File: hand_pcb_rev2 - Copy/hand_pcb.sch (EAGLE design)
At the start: 70 parts

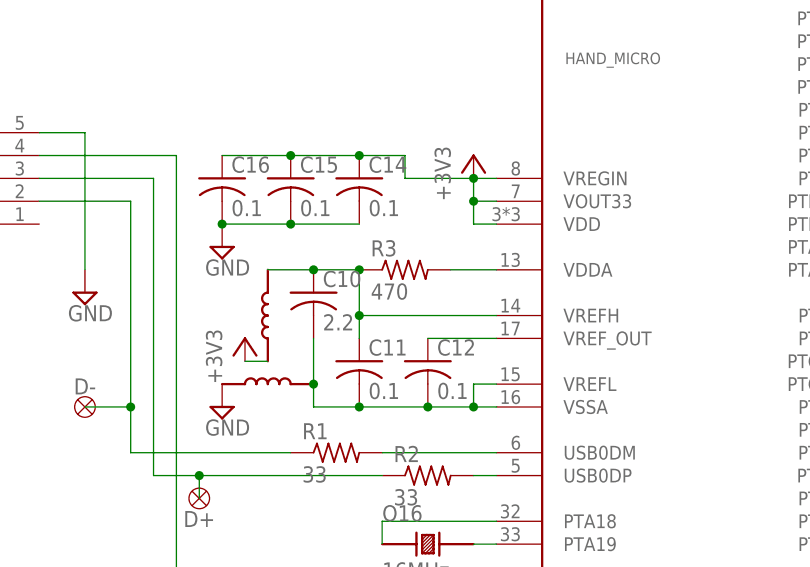
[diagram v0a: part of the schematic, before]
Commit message: corrected some resistors and caps for the M04
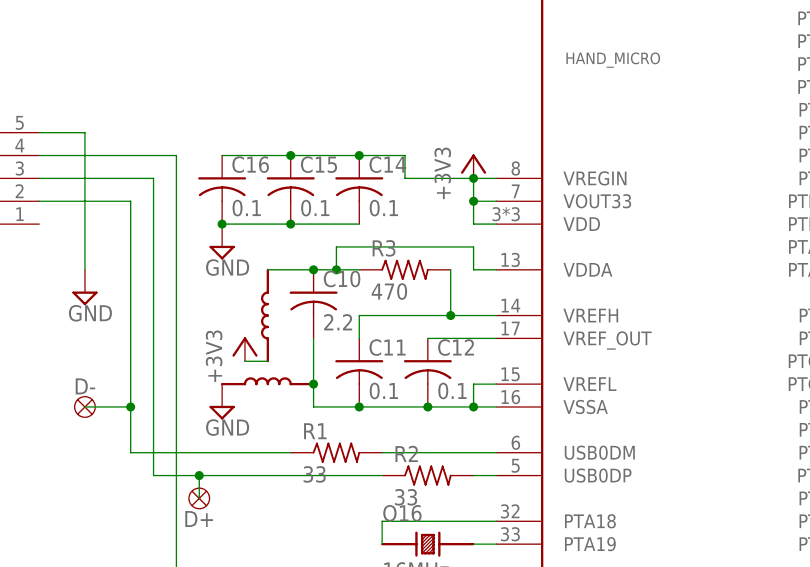
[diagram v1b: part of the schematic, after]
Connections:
- removed net N$32: HAND_MICRO.VDDA, R3.2
- removed net N$33: C10.1, C11.1, HAND_MICRO.VREFH, R3.1, U$4.P$2
- new net N$7: C10.1, HAND_MICRO.VDDA, R3.1, U$4.P$2
- new net N$9: C11.1, HAND_MICRO.VREFH, R3.2
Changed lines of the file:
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@@
-</segment>
-</net>
-<net name="N$32" class="0">
-<segment>
-<pinref part="HAND_MICRO" gate="G$1" pin="VDDA"/>
-<pinref part="R3" gate="G$1" pin="2"/>
-<wire x1="43.18" y1="109.22" x2="48.26" y2="109.22" width="0.1524" layer="91"/>
-</segment>
-</net>
-<net name="N$33" class="0">
-<segment>
-<pinref part="R3" gate="G$1" pin="1"/>
-<wire x1="33.02" y1="101.6" x2="33.02" y2="104.14" width="0.1524" layer="91"/>
-<pinref part="C10" gate="G$1" pin="1"/>
-<wire x1="33.02" y1="104.14" x2="33.02" y2="109.22" width="0.1524" layer="91"/>
-<wire x1="33.02" y1="109.22" x2="27.94" y2="109.22" width="0.1524" layer="91"/>
-<junction x="33.02" y="109.22"/>
-<pinref part="C11" gate="G$1" pin="1"/>
-<pinref part="HAND_MICRO" gate="G$1" pin="VREFH"/>
-<wire x1="48.26" y1="104.14" x2="33.02" y2="104.14" width="0.1524" layer="91"/>
-<junction x="33.02" y="104.14"/>
-<pinref part="U$4" gate="G$1" pin="P$2"/>
-<wire x1="27.94" y1="109.22" x2="22.86" y2="109.22" width="0.1524" layer="91"/>
-<junction x="27.94" y="109.22"/>
 </segment>
 </net>
@@
 </segment>
 </net>
+<net name="N$7" class="0">
+<segment>
+<pinref part="R3" gate="G$1" pin="1"/>
+<pinref part="C10" gate="G$1" pin="1"/>
+<wire x1="33.02" y1="109.22" x2="30.48" y2="109.22" width="0.1524" layer="91"/>
+<pinref part="U$4" gate="G$1" pin="P$2"/>
+<wire x1="30.48" y1="109.22" x2="27.94" y2="109.22" width="0.1524" layer="91"/>
+<wire x1="27.94" y1="109.22" x2="22.86" y2="109.22" width="0.1524" layer="91"/>
+<junction x="27.94" y="109.22"/>
+<pinref part="HAND_MICRO" gate="G$1" pin="VDDA"/>
+<wire x1="48.26" y1="109.22" x2="45.72" y2="109.22" width="0.1524" layer="91"/>
+<wire x1="45.72" y1="109.22" x2="45.72" y2="111.76" width="0.1524" layer="91"/>
+<wire x1="45.72" y1="111.76" x2="30.48" y2="111.76" width="0.1524" layer="91"/>
+<wire x1="30.48" y1="111.76" x2="30.48" y2="109.22" width="0.1524" layer="91"/>
+<junction x="30.48" y="109.22"/>
+</segment>
+</net>
+<net name="N$9" class="0">
+<segment>
+<pinref part="R3" gate="G$1" pin="2"/>
+<pinref part="HAND_MICRO" gate="G$1" pin="VREFH"/>
+<wire x1="48.26" y1="104.14" x2="43.18" y2="104.14" width="0.1524" layer="91"/>
+<wire x1="43.18" y1="104.14" x2="43.18" y2="109.22" width="0.1524" layer="91"/>
+<junction x="43.18" y="104.14"/>
+<wire x1="43.18" y1="104.14" x2="33.02" y2="104.14" width="0.1524" layer="91"/>
+<wire x1="33.02" y1="101.6" x2="33.02" y2="104.14" width="0.1524" layer="91"/>
+<pinref part="C11" gate="G$1" pin="1"/>
+</segment>
+</net>

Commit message: fixed bootloader
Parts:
- BOOTLOADER: value MKL02Z32 -> MKL02Z32CORRECT; device 445-eagle-lib:MKL02Z32 -> 445-eagle-lib:MKL02Z32CORRECT
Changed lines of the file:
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@@
 <part name="THMB" library="445-eagle-lib" deviceset="DRV8833" device=""/>
 <part name="HAND_MICRO" library="445-eagle-lib" deviceset="MK20DX256VLH7" device=""/>
-<part name="BOOTLOADER" library="445-eagle-lib" deviceset="MKL02Z32" device=""/>
+<part name="BOOTLOADER" library="445-eagle-lib" deviceset="MKL02Z32" device="CORRECT" value="MKL02Z32CORRECT"/>
 <part name="+3V1" library="supply1" deviceset="+3V3" device=""/>
 <part name="P+1" library="supply1" deviceset="+5V" device=""/>
@@
 <segment>
 <pinref part="SUPPLY3" gate="GND" pin="GND"/>
-<pinref part="BOOTLOADER" gate="G$1" pin="VSS"/>
 <wire x1="-22.86" y1="35.56" x2="-22.86" y2="40.64" width="0.1524" layer="91"/>
 <pinref part="GND" gate="G$1" pin="P$1"/>
-<wire x1="-22.86" y1="40.64" x2="-22.86" y2="43.18" width="0.1524" layer="91"/>
 <wire x1="-27.94" y1="40.64" x2="-22.86" y2="40.64" width="0.1524" layer="91"/>
+<pinref part="BOOTLOADER" gate="G$1" pin="VSS"/>
+<wire x1="-22.86" y1="43.18" x2="-22.86" y2="40.64" width="0.1524" layer="91"/>
 <junction x="-22.86" y="40.64"/>
 </segment>
@@
 <junction x="309.88" y="73.66"/>
 <pinref part="+3V9" gate="G$1" pin="+3V3"/>
-</segment>
-<segment>
-<pinref part="BOOTLOADER" gate="G$1" pin="VDD"/>
-<pinref part="+3V2" gate="G$1" pin="+3V3"/>
-<wire x1="-22.86" y1="60.96" x2="-22.86" y2="76.2" width="0.1524" layer="91"/>
 </segment>
 <segment>
@@
 <wire x1="-30.48" y1="7.62" x2="-30.48" y2="5.08" width="0.1524" layer="91"/>
 </segment>
+<segment>
+<pinref part="+3V2" gate="G$1" pin="+3V3"/>
+<pinref part="BOOTLOADER" gate="G$1" pin="VDD"/>
+<wire x1="-22.86" y1="76.2" x2="-22.86" y2="60.96" width="0.1524" layer="91"/>
+</segment>
 </net>
 <net name="IDX1" class="0">
@@
 </segment>
 </net>
-<net name="N$13" class="0">
-<segment>
-<pinref part="BOOTLOADER" gate="G$1" pin="PTA7"/>
-<pinref part="HAND_MICRO" gate="G$1" pin="PTA3"/>
-<wire x1="12.7" y1="60.96" x2="48.26" y2="60.96" width="0.1524" layer="91"/>
-</segment>
-</net>
-<net name="N$14" class="0">
-<segment>
-<pinref part="BOOTLOADER" gate="G$1" pin="PTB0"/>
-<pinref part="HAND_MICRO" gate="G$1" pin="PTA0"/>
-<wire x1="12.7" y1="58.42" x2="48.26" y2="58.42" width="0.1524" layer="91"/>
-</segment>
-</net>
-<net name="N$15" class="0">
-<segment>
-<pinref part="BOOTLOADER" gate="G$1" pin="PTB1"/>
-<pinref part="HAND_MICRO" gate="G$1" pin="PTA2"/>
-<wire x1="12.7" y1="55.88" x2="48.26" y2="55.88" width="0.1524" layer="91"/>
-</segment>
-</net>
 <net name="N$17" class="0">
 <segment>
@@
 <wire x1="48.26" y1="48.26" x2="40.64" y2="48.26" width="0.1524" layer="91"/>
 <wire x1="40.64" y1="48.26" x2="40.64" y2="50.8" width="0.1524" layer="91"/>
-<pinref part="BOOTLOADER" gate="G$1" pin="PTB5"/>
 <wire x1="40.64" y1="50.8" x2="15.24" y2="50.8" width="0.1524" layer="91"/>
 <pinref part="BOOTLOADER" gate="G$1" pin="PTA4"/>
-<wire x1="15.24" y1="50.8" x2="12.7" y2="50.8" width="0.1524" layer="91"/>
 <wire x1="12.7" y1="53.34" x2="15.24" y2="53.34" width="0.1524" layer="91"/>
 <wire x1="15.24" y1="53.34" x2="15.24" y2="50.8" width="0.1524" layer="91"/>
+<pinref part="BOOTLOADER" gate="G$1" pin="PTB5"/>
+<wire x1="15.24" y1="50.8" x2="12.7" y2="50.8" width="0.1524" layer="91"/>
 <junction x="15.24" y="50.8"/>
 </segment>
@@
 </segment>
 </net>
-<net name="N$31" class="0">
-<segment>
-<pinref part="RST" gate="G$1" pin="P$1"/>
-<pinref part="BOOTLOADER" gate="G$1" pin="PTB2"/>
-<wire x1="-25.4" y1="50.8" x2="-22.86" y2="50.8" width="0.1524" layer="91"/>
-</segment>
-</net>
 <net name="MIDPWM2" class="0">
 <segment>
@@
 <wire x1="12.7" y1="68.58" x2="-25.4" y2="68.58" width="0.1524" layer="91"/>
 <wire x1="-25.4" y1="68.58" x2="-25.4" y2="53.34" width="0.1524" layer="91"/>
+<wire x1="12.7" y1="121.92" x2="12.7" y2="68.58" width="0.1524" layer="91"/>
+<junction x="12.7" y="68.58"/>
 <pinref part="BOOTLOADER" gate="G$1" pin="PTA6"/>
 <wire x1="-25.4" y1="53.34" x2="-22.86" y2="53.34" width="0.1524" layer="91"/>
-<wire x1="12.7" y1="121.92" x2="12.7" y2="68.58" width="0.1524" layer="91"/>
-<junction x="12.7" y="68.58"/>
 </segment>
 </net>
@@
 </segment>
 </net>
+<net name="N$8" class="0">
+<segment>
+<pinref part="BOOTLOADER" gate="G$1" pin="PTB1"/>
+<pinref part="HAND_MICRO" gate="G$1" pin="PTA2"/>
+<wire x1="12.7" y1="55.88" x2="48.26" y2="55.88" width="0.1524" layer="91"/>
+</segment>
+</net>
+<net name="N$10" class="0">
+<segment>
+<pinref part="HAND_MICRO" gate="G$1" pin="PTA0"/>
+<pinref part="BOOTLOADER" gate="G$1" pin="PTB0"/>
+<wire x1="48.26" y1="58.42" x2="12.7" y2="58.42" width="0.1524" layer="91"/>
+</segment>
+</net>
+<net name="N$11" class="0">
+<segment>
+<pinref part="BOOTLOADER" gate="G$1" pin="PTA7"/>
+<pinref part="HAND_MICRO" gate="G$1" pin="PTA3"/>
+<wire x1="12.7" y1="60.96" x2="48.26" y2="60.96" width="0.1524" layer="91"/>
+</segment>
+</net>
+<net name="N$12" class="0">
+<segment>
+<pinref part="RST" gate="G$1" pin="P$1"/>
+<pinref part="BOOTLOADER" gate="G$1" pin="PTB2"/>
+<wire x1="-25.4" y1="50.8" x2="-22.86" y2="50.8" width="0.1524" layer="91"/>
+</segment>
+</net>

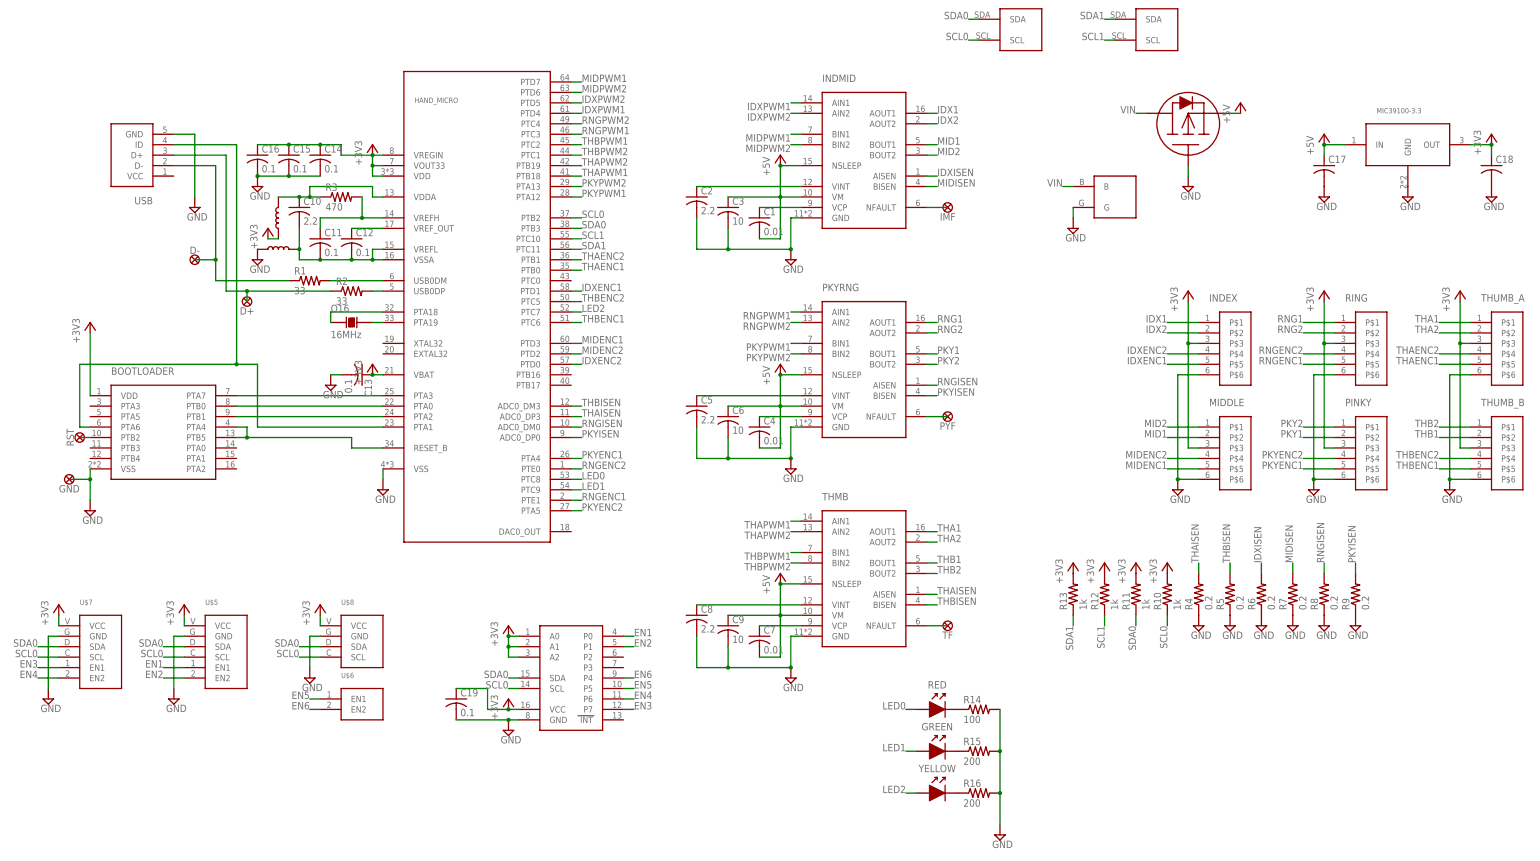
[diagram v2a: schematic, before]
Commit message: updated capacitor values for bypass caps to 10u, cleaned up schematic, updated tanalum cap value for linear regulator
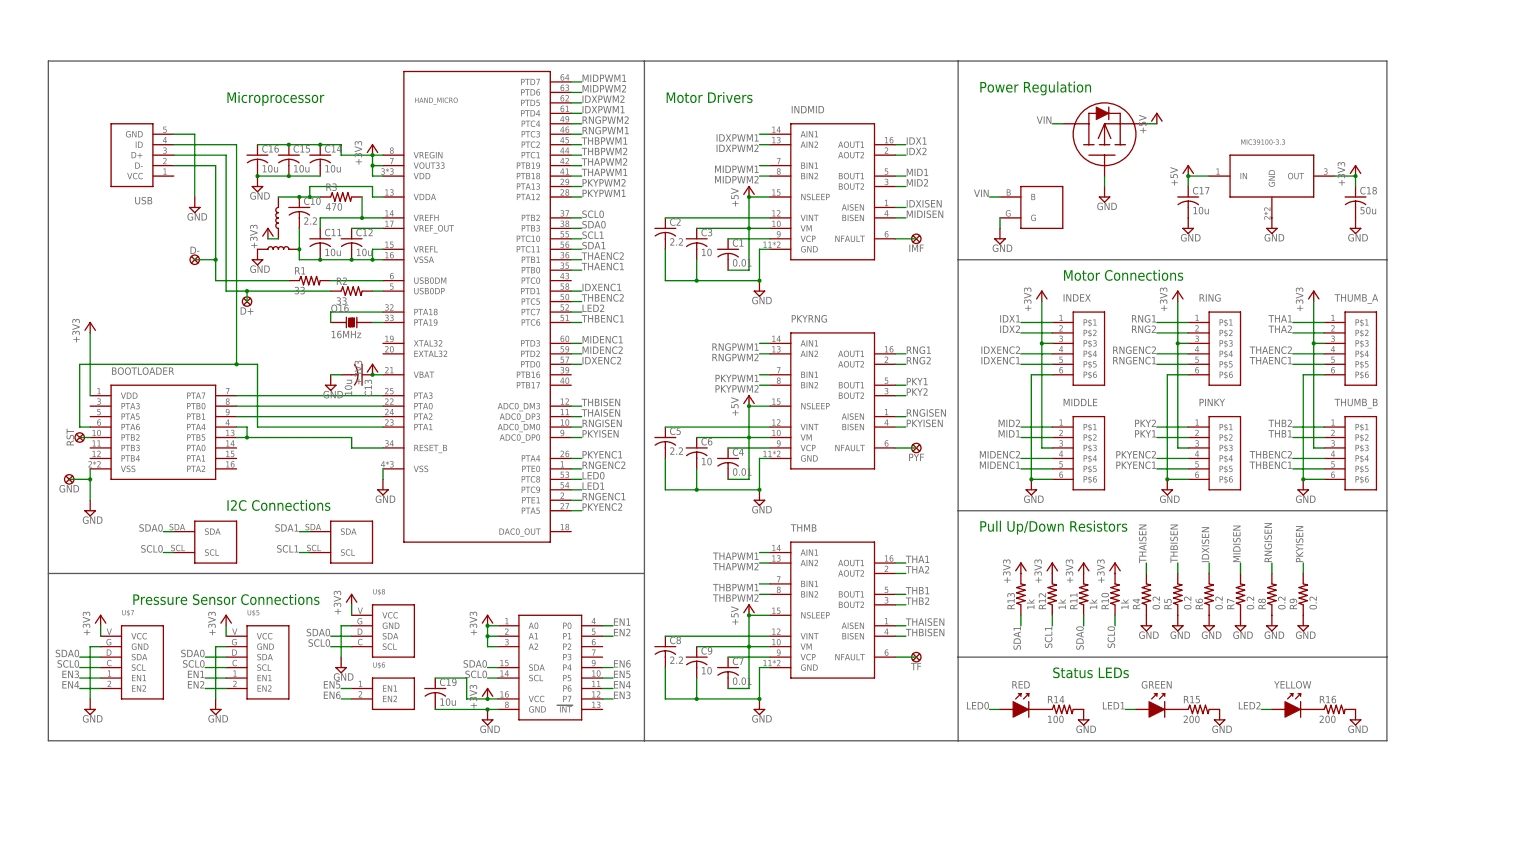
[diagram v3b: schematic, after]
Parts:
- C11, C12, C13, C14, C15, C16, C19: value 0.1 -> 10u
- C17: value (none) -> 10u
- C18: value (none) -> 50u
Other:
- note added: "I2C Connections"
- note added: "Microprocessor"
- note added: "Motor Connections"
- note added: "Motor Drivers"
- note added: "Power Regulation"
- note added: "Pressure Sensor Connections"
- note added: "Pull Up/Down Resistors"
- note added: "Status LEDs"
- moved on the sheet: C1, C17, C18, C19, C2, C3, C4, C5, C6, C7, C8, C9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
